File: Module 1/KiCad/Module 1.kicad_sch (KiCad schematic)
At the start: 19 parts, among them J1 CablesIN, J2 CablesOUT, J3 Resistors, J4 ResGND

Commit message: Updated schematic for Module 1
Added a 5V power flag to the 5V Arduino pin
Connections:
- net +5V: now also A1.5 (5V), R1.1, R2.1, R3.1, R4.1
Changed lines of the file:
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@@
+	)
+	(junction
+		(at 102.87 92.71)
+		(diameter 0)
+		(color 0 0 0 0)
 	)
 	(junction
@@
 					(unit 1)
 				)
+			)
+		)
+	)
+	(symbol
+		(lib_id "power:+5V")
+		(at 102.87 92.71 90)
+		(unit 1)
+		(exclude_from_sim no)
+		(in_bom yes)
+		(on_board yes)
+		(dnp no)
+		(property "Reference" "#PWR04"
+			(at 106.68 92.71 0)
+			(effects
+				(font
+					(size 1.27 1.27)
+				)
+				(hide yes)
+			)
+		)
+		(property "Value" "+5V"
+			(at 99.822 92.71 90)
+			(effects
+				(font
+					(size 1.27 1.27)
+				)
+				(justify left)
+			)
+		)
+		(property "Footprint" ""
+			(at 102.87 92.71 0)
+			(effects
+				(font
+					(size 1.27 1.27)
+				)
+				(hide yes)
+			)
+		)
+		(property "Datasheet" ""
+			(at 102.87 92.71 0)
+			(effects
+				(font
+					(size 1.27 1.27)
+				)
+				(hide yes)
+			)
+		)
+		(property "Description" "Power symbol creates a global label with name \"+5V\""
+			(at 102.87 92.71 0)
+			(effects
+				(font
+					(size 1.27 1.27)
+				)
+				(hide yes)
+			)
+		)
+		(pin "1"
+		)
+		(instances
+			(project "Module 1"
+				(path "/8aed8e43-d237-4a6d-a7fe-22d8baa8c839"
+					(reference "#PWR04")
+					(unit 1)
+				)

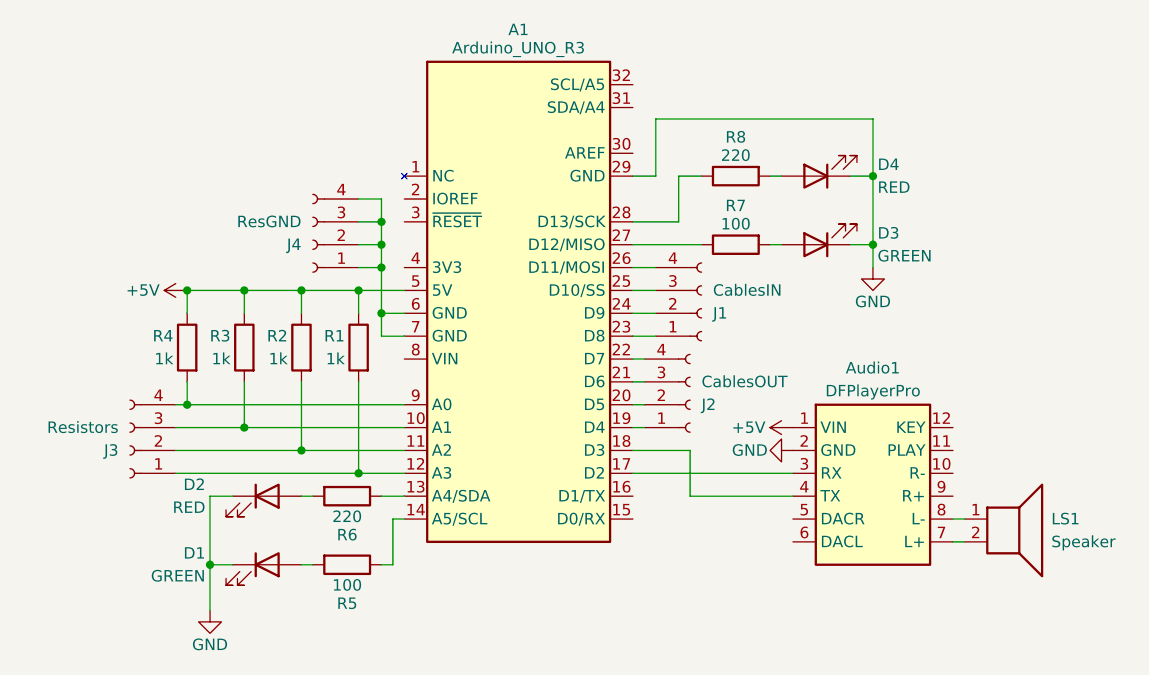
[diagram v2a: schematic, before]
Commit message: Updated Module 1 schematic
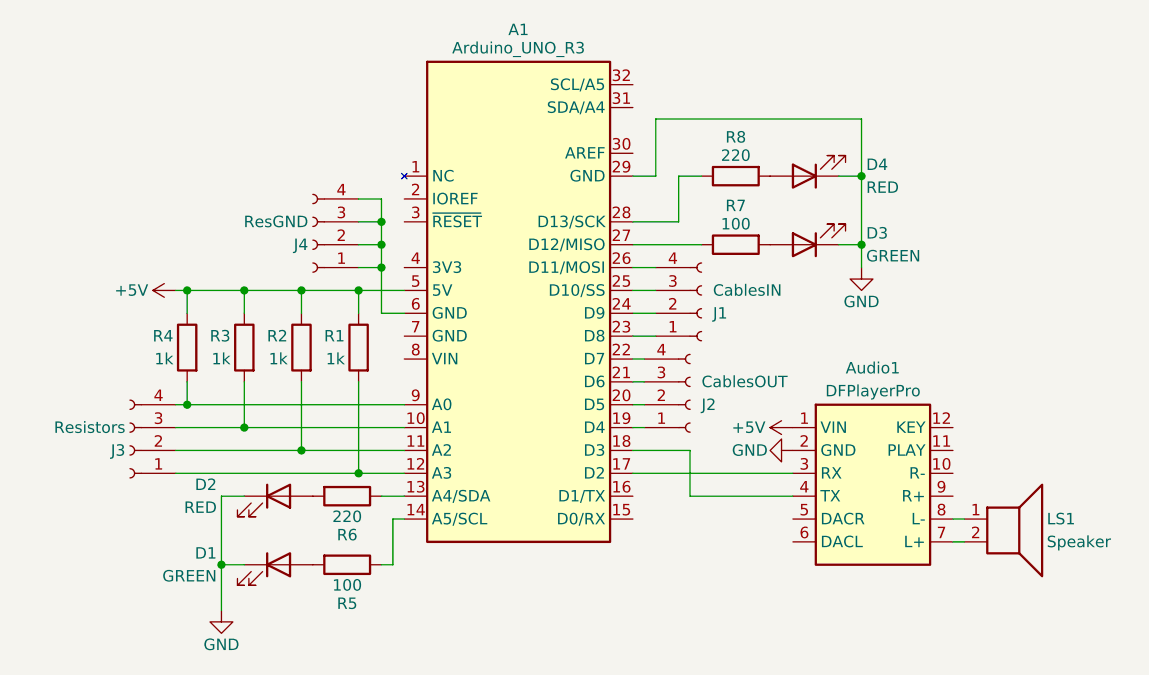
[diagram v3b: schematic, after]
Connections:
- net at A1.6 (GND), J4.1 (Pin_1), J4.2 (Pin_2)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: no longer A1.7 (GND)
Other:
- moved on the sheet: D1, D2, D3, D4
